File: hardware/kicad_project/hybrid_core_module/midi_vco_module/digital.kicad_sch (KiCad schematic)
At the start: 47 parts, among them Q2 BC848, Q3 BC848, SW4 SW_Push, SW5 SW_Push, U1 SHT4x, U10 CP2102N-Axx-xQFN28, U17 SHT4x, U9 ESP32-WROOM-32E

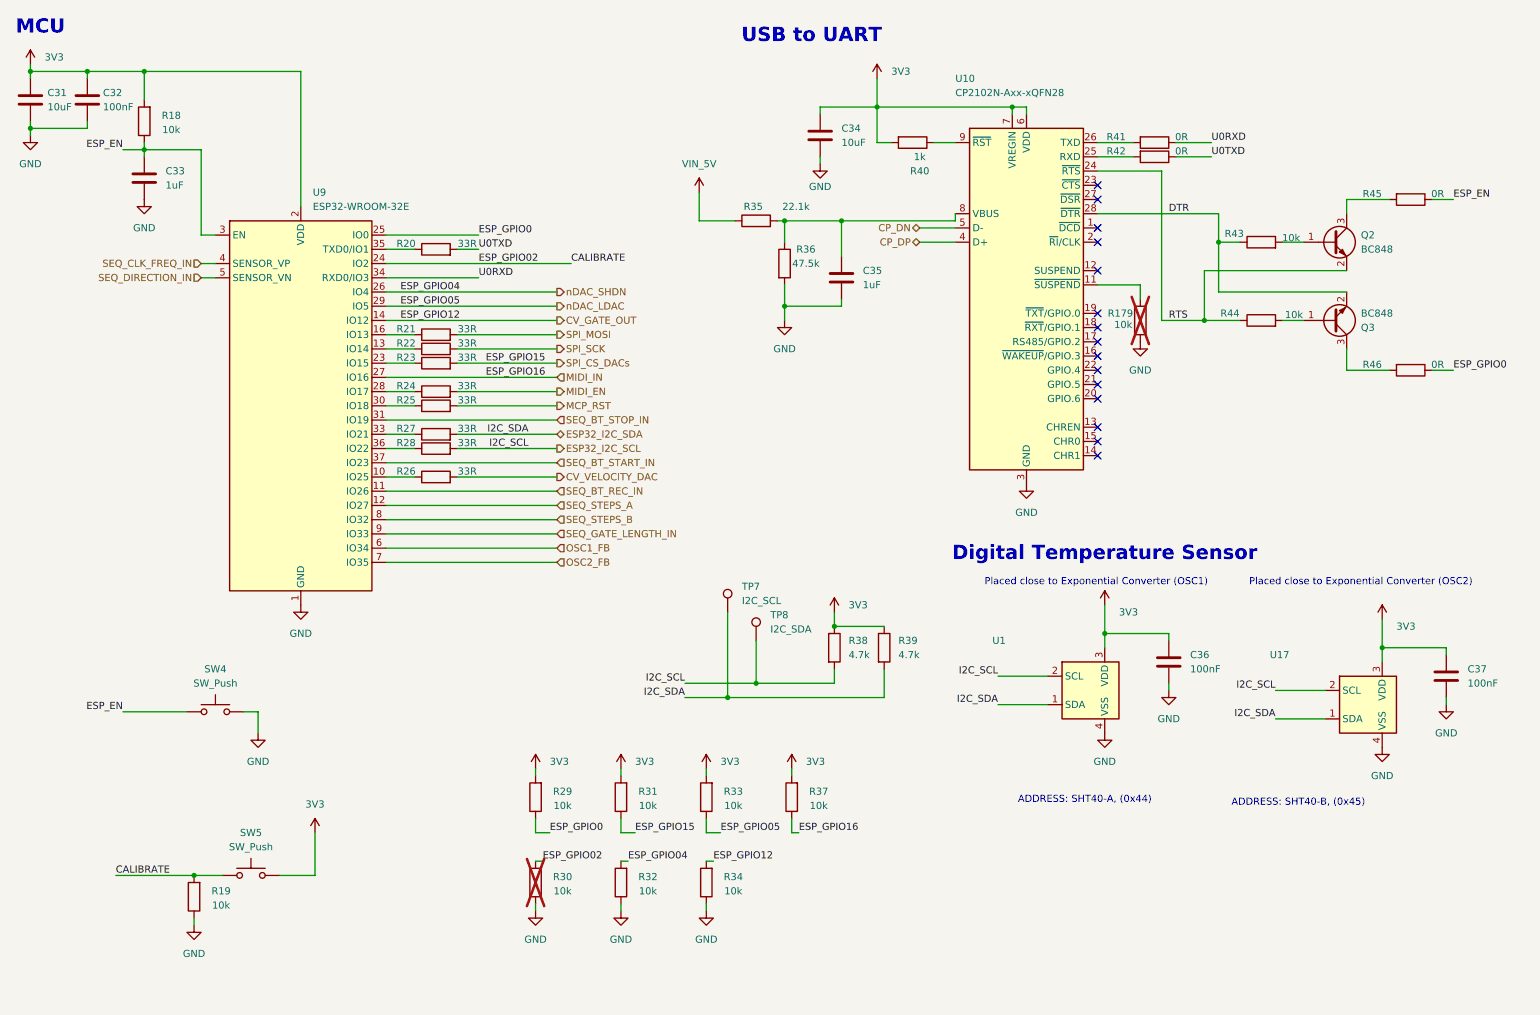
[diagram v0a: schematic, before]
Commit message: Schematic updated. Components Footprint assignment started. Waiting for components mechanical validation before starting layout.
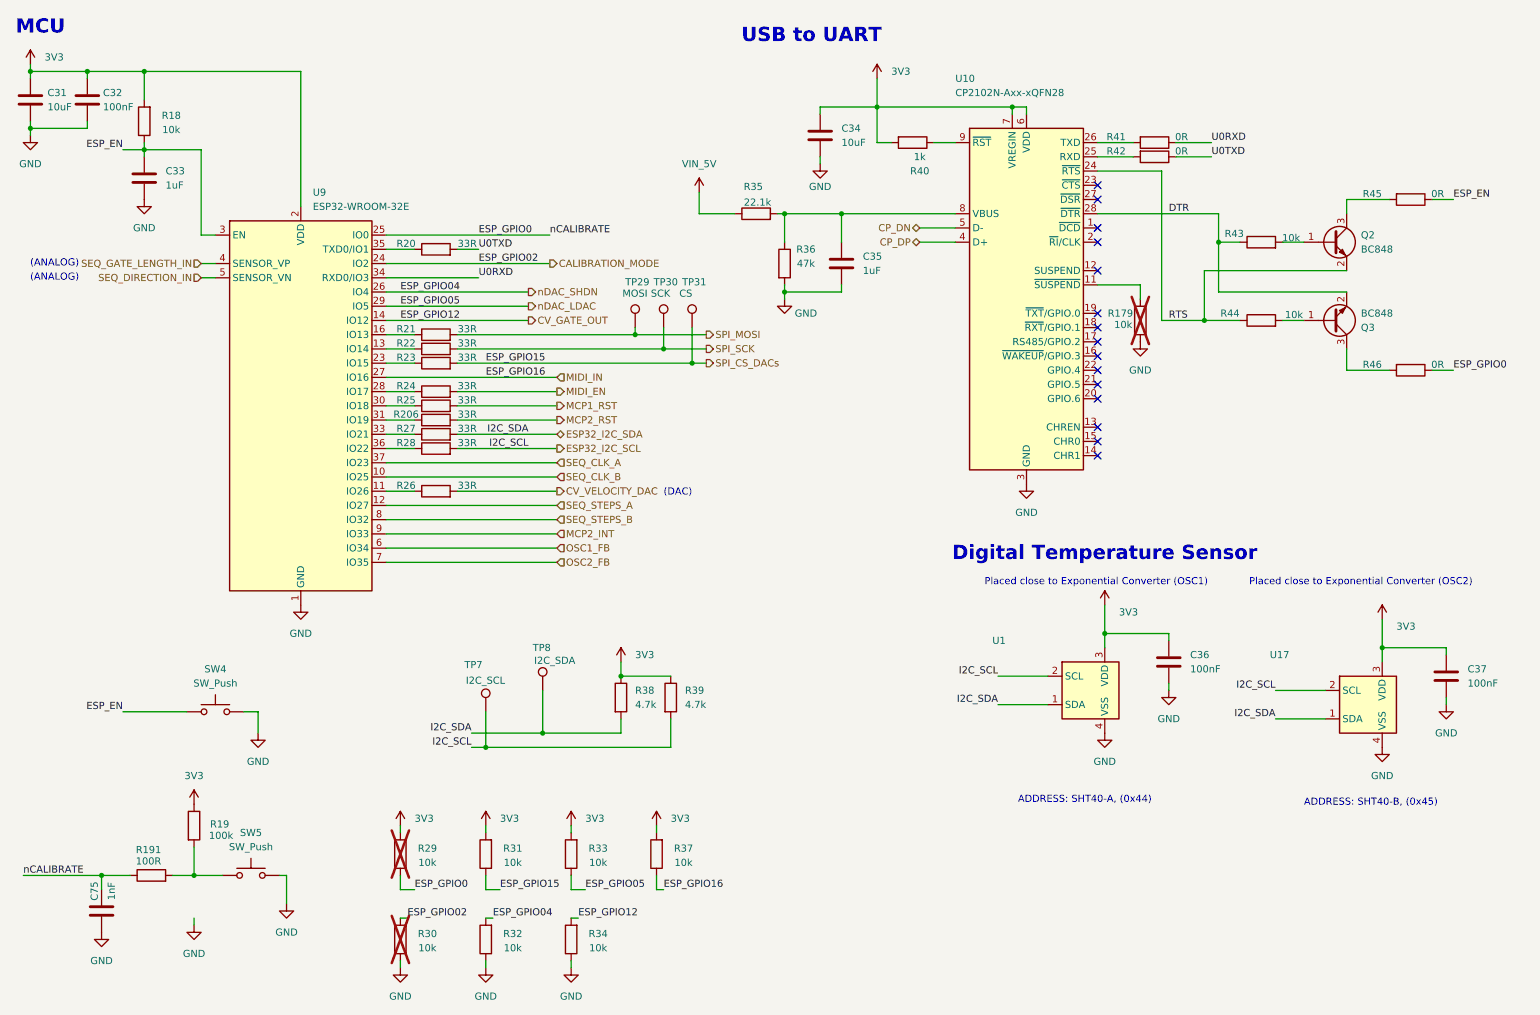
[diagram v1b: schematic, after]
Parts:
- added C75: 1nF, Capacitor_SMD:C_0402_1005Metric, symbol Device:C
- added R191: 100R, Resistor_SMD:R_0402_1005Metric, symbol Device:R
- added R206: 33R, Resistor_SMD:R_0402_1005Metric, symbol Device:R
- added TP29: MOSI, symbol Connector:TestPoint
- added TP30: SCK, symbol Connector:TestPoint
- added TP31: CS, symbol Connector:TestPoint
- C31, C34: footprint Capacitor_SMD:C_0402_1005Metric -> Capacitor_SMD:C_0805_2012Metric; Manufacturer (none) -> MURATA; Manufacturer PartNumer (none) -> GRM21BR61E106KA73K
- C32, C36, C37: footprint (none) -> Capacitor_SMD:C_0402_1005Metric; Manufacturer (none) -> MURATA; Manufacturer PartNumer (none) -> GRM155R71E104KE14J
- C33, C35: footprint (none) -> Capacitor_SMD:C_0805_2012Metric; Manufacturer (none) -> MURATA; Manufacturer PartNumer (none) -> GRM219R71E105MA88J
- R179, R18, R30, R31, R32, R33, R34, R37, R43, R44: footprint (none) -> Resistor_SMD:R_0402_1005Metric; Manufacturer (none) -> YAGEO; Manufacturer PartNumer (none) -> RT0402FRE0710KL
- R19: value 10k -> 100k; footprint (none) -> Resistor_SMD:R_0402_1005Metric; Manufacturer (none) -> YAGEO; Manufacturer PartNumer (none) -> RT0402FRE07100KL
- R20, R21, R22, R23, R24, R25, R26, R27, R28: footprint (none) -> Resistor_SMD:R_0402_1005Metric; Manufacturer (none) -> YAGEO; Manufacturer PartNumer (none) -> RT0402FRE0733RL
- R29: footprint (none) -> Resistor_SMD:R_0402_1005Metric; Manufacturer (none) -> YAGEO; Manufacturer PartNumer (none) -> RT0402FRE0710KL; now not fitted
- R35: footprint (none) -> Resistor_SMD:R_0402_1005Metric; Manufacturer (none) -> YAGEO; Manufacturer PartNumer (none) -> RT0402FRE0721KL
- R36: value 47.5k -> 47k; footprint (none) -> Resistor_SMD:R_0402_1005Metric; Manufacturer (none) -> YAGEO; Manufacturer PartNumer (none) -> RT0402FRE0747KL
- R38, R39: footprint (none) -> Resistor_SMD:R_0402_1005Metric; Manufacturer (none) -> YAGEO; Manufacturer PartNumer (none) -> RT0402FRE074K7L
- R40: footprint (none) -> Resistor_SMD:R_0402_1005Metric; Manufacturer (none) -> YAGEO; Manufacturer PartNumer (none) -> RT0402FRE071KL
- R41, R42, R45, R46: footprint (none) -> Resistor_SMD:R_0402_1005Metric; Manufacturer (none) -> YAGEO; Manufacturer PartNumer (none) -> RC0402FR-070RL
- TP7, TP8: now left out of the parts list
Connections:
- net SEQ_BT_REC_IN is gone; now on an unnamed net: U9.11 (IO26)
- net SEQ_CLK_FREQ_IN is gone; now on net SEQ_GATE_LENGTH_IN: U9.4 (SENSOR_VP)
- net 3V3: now also R19.1; no longer SW5.2
- net ESP32_I2C_SCL: now also R39.2, TP7.1; no longer R38.2, TP8.1
- net ESP32_I2C_SDA: now also R38.2, TP8.1; no longer R39.2, TP7.1
- net ESP_GPIO0: now also C75.2, R191.1
- net GND: now also SW5.2, C75.1; no longer R19.1
- net SEQ_GATE_LENGTH_IN: no longer U9.9 (IO33)
- net SPI_CS_DACs: now also TP31.1
- net SPI_MOSI: now also TP29.1
- net SPI_SCK: now also TP30.1
- net at R26.1: no longer U9.10 (IO25)
- net CALIBRATE: no longer names the net of R19.2, SW5.1
- net CALIBRATE: now also R191.2; no longer R30.2, U9.24 (IO2)
- net MCP_RST renamed MCP1_RST
- net SEQ_BT_START_IN renamed SEQ_CLK_A
- net SEQ_BT_STOP_IN: no longer names the net of U9.31 (IO19)
- net SEQ_BT_STOP_IN: now also R206.1
- new net CALIBRATION_MODE: R30.2, U9.24 (IO2)
- new net MCP2_INT: U9.9 (IO33)
- new net MCP2_RST: R206.2
- new net SEQ_CLK_B: U9.10 (IO25)
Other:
- note added: "(ANALOG)"
- note added: "(DAC)"
- moved on the sheet: C35, R26, R30, R31, R32, R33, R34, R35, R37, R38, R39, TP7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

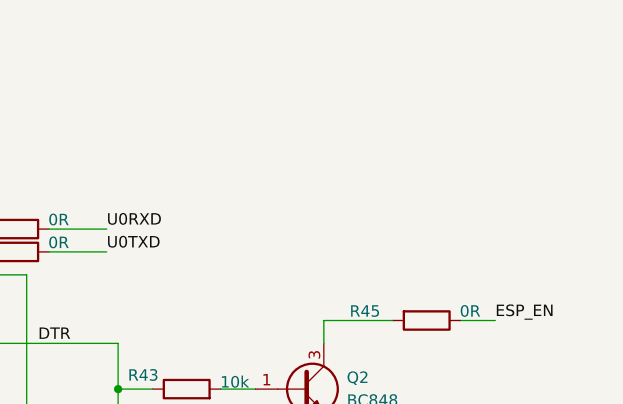
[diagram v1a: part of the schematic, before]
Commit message: - schematic updated  - PN and footprints added
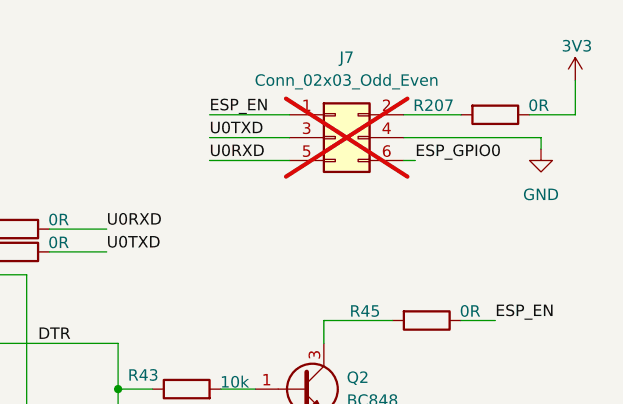
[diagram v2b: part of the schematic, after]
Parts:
- added J7: Conn_02x03_Odd_Even, Connector_PinHeader_1.27mm:PinHeader_2x03_P1.27mm_Vertical_SMD, symbol Connector_Generic:Conn_02x03_Odd_Even
- added R207: 0R, Resistor_SMD:R_0402_1005Metric, symbol Device:R
- Q2, Q3: Manufacturer (none) -> Fairchild Semiconductor; Manufacturer PartNumer (none) -> BC848A
- SW4, SW5: footprint (none) -> Button_Switch_THT:SW_PUSH_6mm
- U10: Manufacturer (none) -> Silicon Labs; Manufacturer PartNumer (none) -> CP2102N-A02-GQFN28R
- U9: Manufacturer (none) -> Espressif Systems; Manufacturer PartNumer (none) -> ESP32-WROOM-32E-N8
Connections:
- net 3V3: now also R207.1
- net ESP_EN: now also J7.1 (Pin_1)
- net ESP_GPIO0: now also J7.6 (Pin_6)
- net GND: now also J7.4 (Pin_4)
- net U0RXD: now also J7.5 (Pin_5)
- net U0TXD: now also J7.3 (Pin_3)
- new net: J7.2 (Pin_2), R207.2

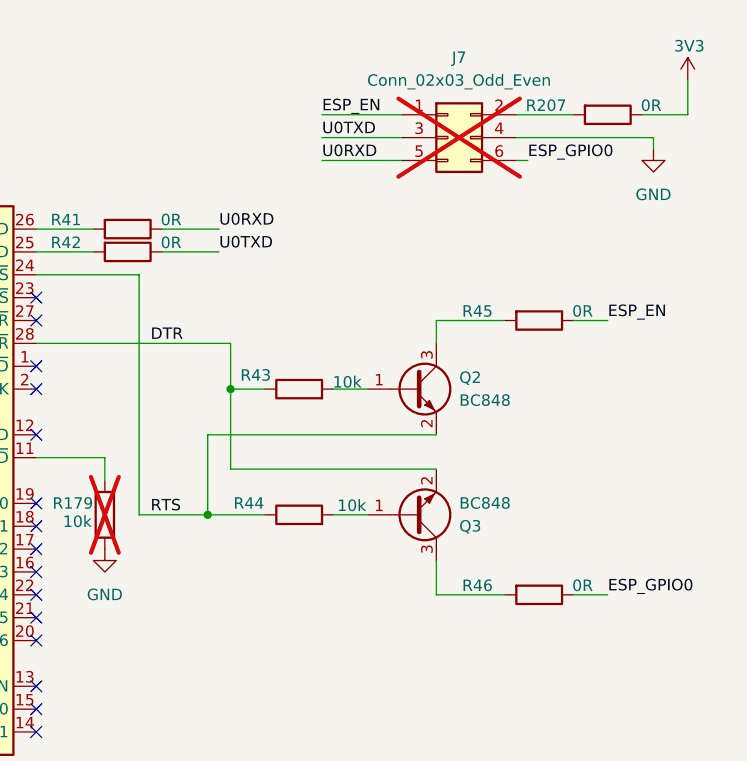
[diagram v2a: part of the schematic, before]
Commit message: components placement (interface) components placement per section
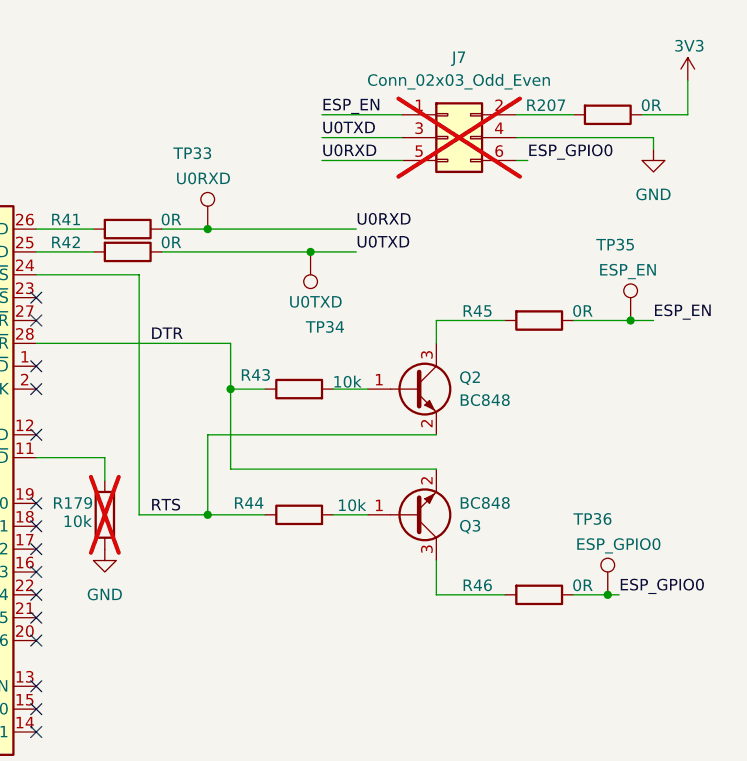
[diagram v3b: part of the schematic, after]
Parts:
- added TP33: U0RXD, TestPoint:TestPoint_Pad_1.0x1.0mm, symbol Connector:TestPoint
- added TP34: U0TXD, TestPoint:TestPoint_Pad_1.0x1.0mm, symbol Connector:TestPoint
- added TP35: ESP_EN, TestPoint:TestPoint_Pad_1.0x1.0mm, symbol Connector:TestPoint
- added TP36: ESP_GPIO0, TestPoint:TestPoint_Pad_1.0x1.0mm, symbol Connector:TestPoint
- TP29, TP30, TP31, TP7, TP8: footprint (none) -> TestPoint:TestPoint_Pad_1.0x1.0mm
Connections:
- net ESP_EN: now also TP35.1
- net ESP_GPIO0: now also TP36.1
- net U0RXD: now also TP33.1
- net U0TXD: now also TP34.1

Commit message: - placement done - routing 60%
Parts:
- R207: now not fitted
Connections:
- net CP_DN renamed CP_D_N
- net CP_DP renamed CP_D_P
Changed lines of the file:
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@@
 	(wire
 		(pts
-			(xy 176.53 53.34) (xy 182.88 53.34)
+			(xy 173.99 53.34) (xy 182.88 53.34)
 		)
 		(stroke
@@
 	(wire
 		(pts
-			(xy 46.99 177.8) (xy 46.99 176.53)
-		)
-		(stroke
-			(width 0)
-			(type default)
-		)
-	)
-	(wire
-		(pts
 			(xy 158.75 41.91) (xy 158.75 40.64)
 		)
@@
 	(wire
 		(pts
-			(xy 176.53 55.88) (xy 182.88 55.88)
+			(xy 173.99 55.88) (xy 182.88 55.88)
 		)
 		(stroke
@@
 		)
 	)
+	(label "CP_D_N"
+		(at 175.26 53.34 0)
+		(effects
+			(font
+				(size 1.27 1.27)
+			)
+			(justify left bottom)
+		)
+	)
 	(label "ESP_GPIO0"
 		(at 97.79 54.61 0)
@@
 		)
 	)
+	(label "CP_D_P"
+		(at 175.26 55.88 0)
+		(effects
+			(font
+				(size 1.27 1.27)
+			)
+			(justify left bottom)
+		)
+	)
 	(label "ESP_GPIO02"
 		(at 85.09 176.53 0)
@@
 		)
 	)
-	(hierarchical_label "CP_DP"
+	(hierarchical_label "CP_D_P"
 		(shape bidirectional)
-		(at 176.53 55.88 180)
+		(at 173.99 55.88 180)
 		(effects
 			(font
@@
 		)
 	)
-	(hierarchical_label "CP_DN"
+	(hierarchical_label "CP_D_N"
 		(shape bidirectional)
-		(at 176.53 53.34 180)
+		(at 173.99 53.34 180)
 		(effects
 			(font
@@
 		(in_bom yes)
 		(on_board yes)
-		(dnp no)
+		(dnp yes)
 		(property "Reference" "R207"
 			(at 264.922 24.384 90)
@@
 					(unit 1)
 				)
-			)
-		)
-	)
-	(symbol
-		(lib_id "power:GND")
-		(at 46.99 177.8 0)
-		(unit 1)
-		(exclude_from_sim no)
-		(in_bom yes)
-		(on_board yes)
-		(dnp no)
-		(fields_autoplaced yes)
-		(property "Reference" "#PWR0170"
-			(at 46.99 184.15 0)
-			(effects
-				(font
-					(size 1.27 1.27)
-				)
-				(hide yes)
-			)
-		)
-		(property "Value" "GND"
-			(at 46.99 182.88 0)
-			(effects
-				(font
-					(size 1.27 1.27)
-				)
-			)
-		)
-		(property "Footprint" ""
-			(at 46.99 177.8 0)
-			(effects
-				(font
-					(size 1.27 1.27)
-				)
-				(hide yes)
-			)
-		)
-		(property "Datasheet" ""
-			(at 46.99 177.8 0)
-			(effects
-				(font
-					(size 1.27 1.27)
-				)
-				(hide yes)
-			)
-		)
-		(property "Description" "Power symbol creates a global label with name \"GND\" , ground"
-			(at 46.99 177.8 0)
-			(effects
-				(font
-					(size 1.27 1.27)
-				)
-				(hide yes)
-			)
-		)
-		(pin "1"
-		)
-		(instances
-			(project "midi_vco_module"
-				(path "/3378c2b5-f4b3-47f0-8cdf-dba4991b82b5/07f03e9d-967e-4db5-8422-4176953ca616"
-					(reference "#PWR0170")
-					(unit 1)
-				)
